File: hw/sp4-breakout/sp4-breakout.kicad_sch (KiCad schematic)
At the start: 8 parts, among them J1 nRF24 header, J2 3V3 bench supply, U1 E01-ML01SP4

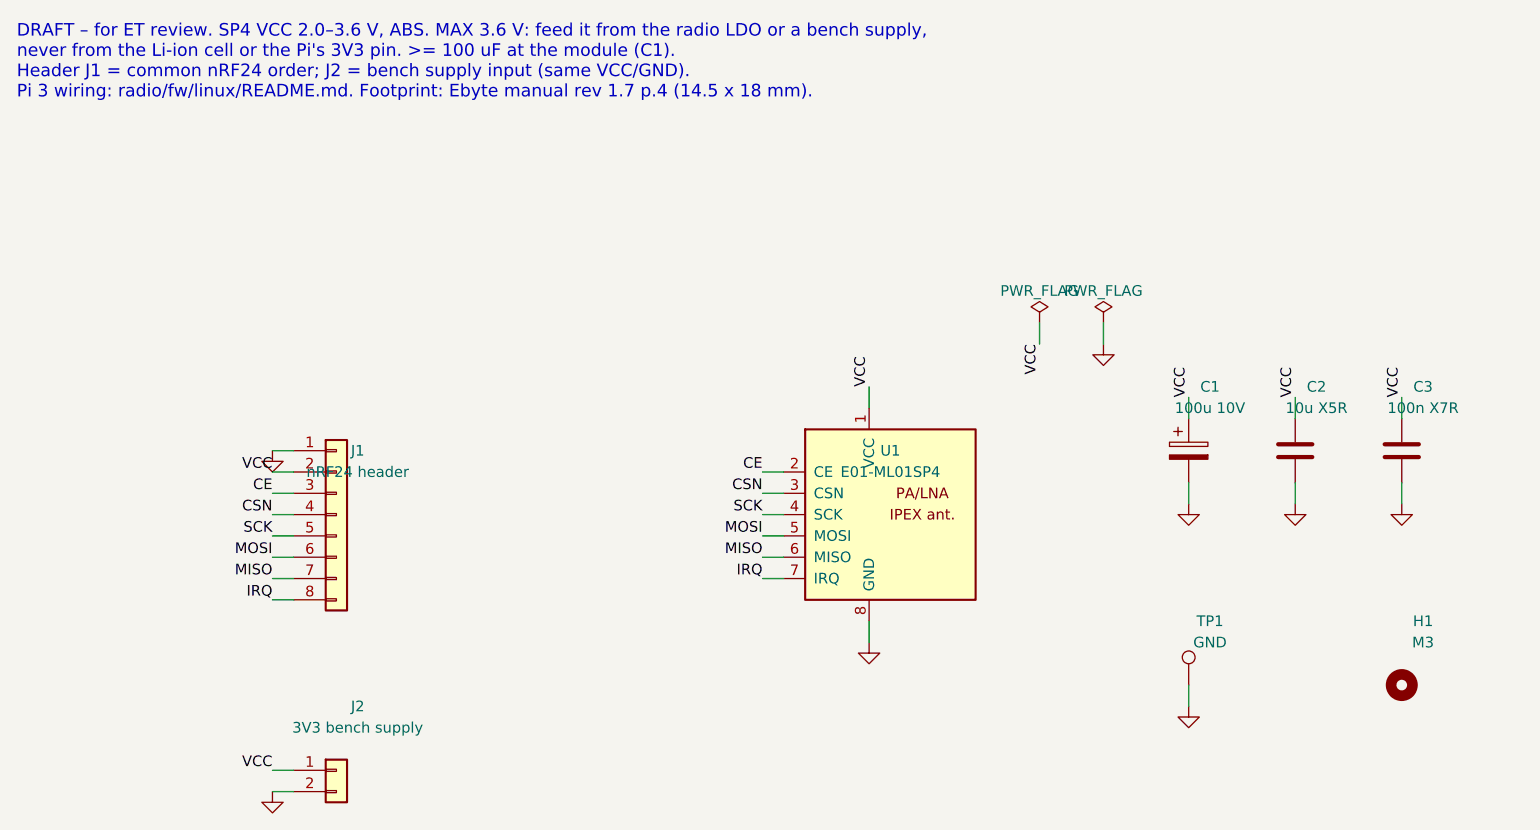
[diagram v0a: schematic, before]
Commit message: SP4 breakout: 2.0 mm header pads and no pour between C1's pads (UPC lab rules)
- J1/J2 use teamc:PinHeader_1x08/1x02_P2.54mm_Vertical_Pad2.0mm, written by
  build_breakout.py from the stock headers (1.7 -> 2.0 mm pads, 1.0 mm drill
  kept, pin 1 square): hole + 1.0 mm, 0.54 mm between pads at 2.54 mm pitch.
  A library copy rather than a board override, so DRC's library-parity check
  stays clean.
- FR10: a no-fill rule area in C1's 2.1 mm pad gap (the only SMD gap the pour
  reached); SP4 castellations and the 0805 gaps had no pour.
- build_breakout.py restores the lab floor (0.3 mm clearance/track, 2 thermal
  spokes) after set_project_rules, which lowered it for the carrier.
- Regenerated board, schematic, fab/ and the gerber zip: ERC 0, DRC 0
  violations / 0 unconnected / 0 parity (all severities). Footprint
  positions and the 30 tracks (0.5/0.6 mm) unchanged.

Co-Authored-By: Claude Opus 5.5 <noreply@anthropic.com>
Claude-Session: https://claude.ai/code/session_01PKzvcoWGaf5niy6TrXYsya
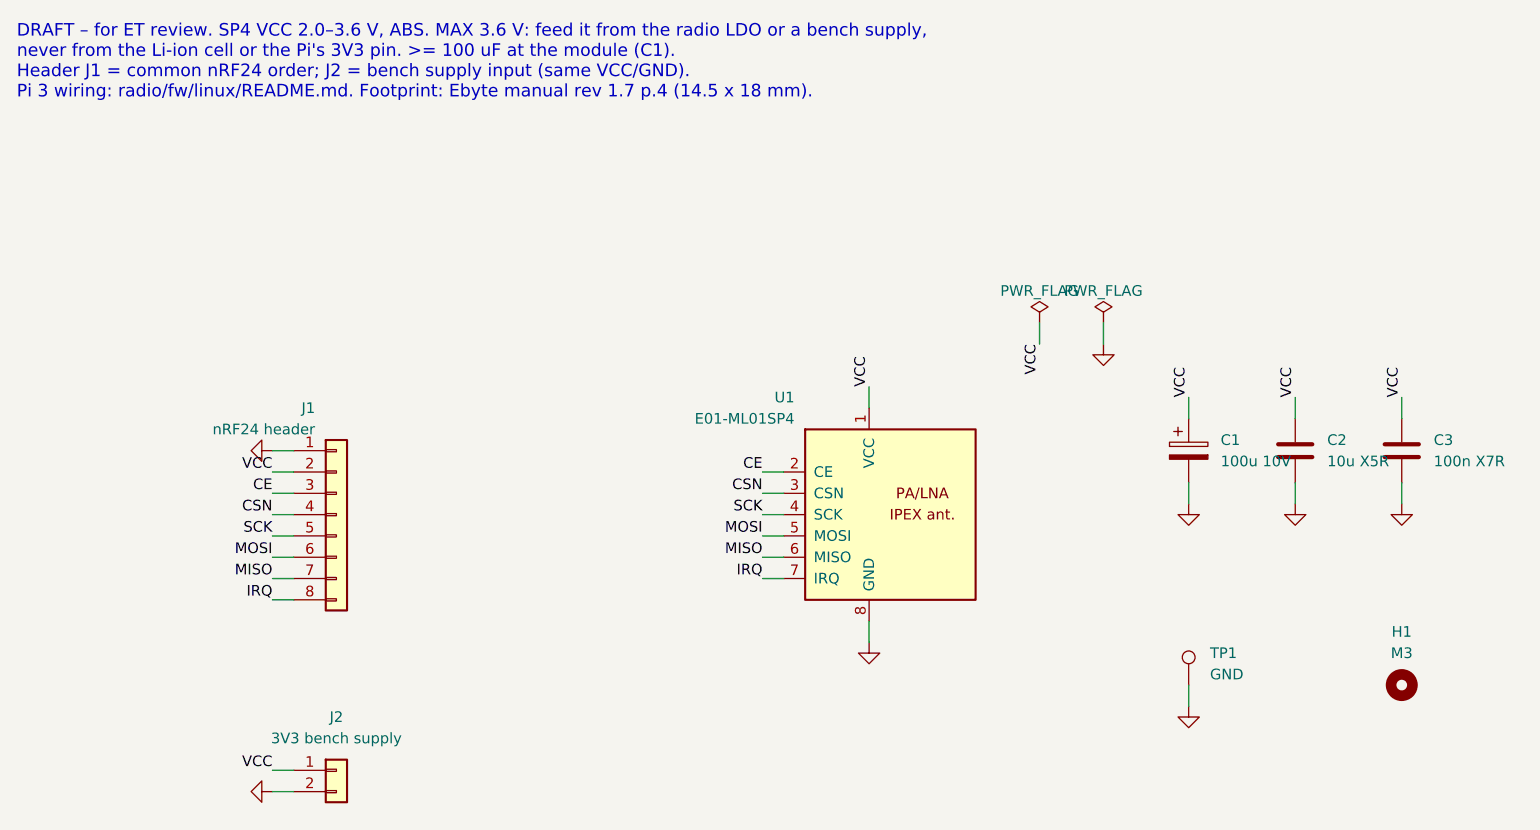
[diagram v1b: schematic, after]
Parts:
- J1: footprint Connector_PinHeader_2.54mm:PinHeader_1x08_P2.54mm_Vertical -> teamc:PinHeader_1x08_P2.54mm_Vertical_Pad2.0mm
- J2: footprint Connector_PinHeader_2.54mm:PinHeader_1x02_P2.54mm_Vertical -> teamc:PinHeader_1x02_P2.54mm_Vertical_Pad2.0mm
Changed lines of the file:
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@@
 		(dnp no)
 		(property "Reference" "U1"
-			(at 129.54 81.28 0)
-			(effects
-				(font
-					(size 1.27 1.27)
-				)
+			(at 118.11 74.93 0)
+			(effects
+				(font
+					(size 1.27 1.27)
+				)
+				(justify right)
 			)
 		)
 		(property "Value" "E01-ML01SP4"
-			(at 129.54 83.82 0)
-			(effects
-				(font
-					(size 1.27 1.27)
-				)
+			(at 118.11 77.47 0)
+			(effects
+				(font
+					(size 1.27 1.27)
+				)
+				(justify right)
 			)
 		)
@@
 	(symbol
 		(lib_id "power:GND")
-		(at 55.88 81.28 0)
+		(at 55.88 81.28 270)
 		(unit 1)
 		(exclude_from_sim no)
@@
 		(dnp no)
 		(property "Reference" "J1"
-			(at 66.04 81.28 0)
-			(effects
-				(font
-					(size 1.27 1.27)
-				)
+			(at 60.96 76.2 0)
+			(effects
+				(font
+					(size 1.27 1.27)
+				)
+				(justify right)
 			)
 		)
 		(property "Value" "nRF24 header"
-			(at 66.04 83.82 0)
-			(effects
-				(font
-					(size 1.27 1.27)
-				)
-			)
-		)
-		(property "Footprint" "Connector_PinHeader_2.54mm:PinHeader_1x08_P2.54mm_Vertical"
+			(at 60.96 78.74 0)
+			(effects
+				(font
+					(size 1.27 1.27)
+				)
+				(justify right)
+			)
+		)
+		(property "Footprint" "teamc:PinHeader_1x08_P2.54mm_Vertical_Pad2.0mm"
 			(at 63.5 88.9 0)
 			(effects
@@
 	(symbol
 		(lib_id "power:GND")
-		(at 55.88 121.92 0)
+		(at 55.88 121.92 270)
 		(unit 1)
 		(exclude_from_sim no)
@@
 		(dnp no)
 		(property "Reference" "J2"
-			(at 66.04 111.76 0)
+			(at 63.5 113.03 0)
 			(effects
 				(font
@@
 		)
 		(property "Value" "3V3 bench supply"
-			(at 66.04 114.3 0)
-			(effects
-				(font
-					(size 1.27 1.27)
-				)
-			)
-		)
-		(property "Footprint" "Connector_PinHeader_2.54mm:PinHeader_1x02_P2.54mm_Vertical"
+			(at 63.5 115.57 0)
+			(effects
+				(font
+					(size 1.27 1.27)
+				)
+			)
+		)
+		(property "Footprint" "teamc:PinHeader_1x02_P2.54mm_Vertical_Pad2.0mm"
 			(at 63.5 119.38 0)
 			(effects
@@
 		(dnp no)
 		(property "Reference" "C1"
-			(at 167.64 73.66 0)
-			(effects
-				(font
-					(size 1.27 1.27)
-				)
+			(at 168.91 80.01 0)
+			(effects
+				(font
+					(size 1.27 1.27)
+				)
+				(justify left)
 			)
 		)
 		(property "Value" "100u 10V"
-			(at 167.64 76.2 0)
-			(effects
-				(font
-					(size 1.27 1.27)
-				)
+			(at 168.91 82.55 0)
+			(effects
+				(font
+					(size 1.27 1.27)
+				)
+				(justify left)
 			)
 		)
@@
 		(dnp no)
 		(property "Reference" "C2"
-			(at 180.34 73.66 0)
-			(effects
-				(font
-					(size 1.27 1.27)
-				)
+			(at 181.61 80.01 0)
+			(effects
+				(font
+					(size 1.27 1.27)
+				)
+				(justify left)
 			)
 		)
 		(property "Value" "10u X5R"
-			(at 180.34 76.2 0)
-			(effects
-				(font
-					(size 1.27 1.27)
-				)
+			(at 181.61 82.55 0)
+			(effects
+				(font
+					(size 1.27 1.27)
+				)
+				(justify left)
 			)
 		)
@@
 		(dnp no)
 		(property "Reference" "C3"
-			(at 193.04 73.66 0)
-			(effects
-				(font
-					(size 1.27 1.27)
-				)
+			(at 194.31 80.01 0)
+			(effects
+				(font
+					(size 1.27 1.27)
+				)
+				(justify left)
 			)
 		)
 		(property "Value" "100n X7R"
-			(at 193.04 76.2 0)
-			(effects
-				(font
-					(size 1.27 1.27)
-				)
+			(at 194.31 82.55 0)
+			(effects
+				(font
+					(size 1.27 1.27)
+				)
+				(justify left)
 			)
 		)
@@
 		(dnp no)
 		(property "Reference" "TP1"
-			(at 167.64 101.6 0)
-			(effects
-				(font
-					(size 1.27 1.27)
-				)
+			(at 167.64 105.41 0)
+			(effects
+				(font
+					(size 1.27 1.27)
+				)
+				(justify left)
 			)
 		)
 		(property "Value" "GND"
-			(at 167.64 104.14 0)
-			(effects
-				(font
-					(size 1.27 1.27)
-				)
+			(at 167.64 107.95 0)
+			(effects
+				(font
+					(size 1.27 1.27)
+				)
+				(justify left)
 			)
 		)
@@
 		(dnp no)
 		(property "Reference" "H1"
-			(at 193.04 101.6 0)
+			(at 190.5 102.87 0)
 			(effects
 				(font
@@
 		)
 		(property "Value" "M3"
-			(at 193.04 104.14 0)
-			(effects
-				(font
+			(at 190.5 105.41 0)
+			(effects
+				(font
